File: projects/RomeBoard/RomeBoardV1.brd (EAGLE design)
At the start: 110 x 130 mm, 15 parts, among them J2 RASPBERRY-PI-HEADER

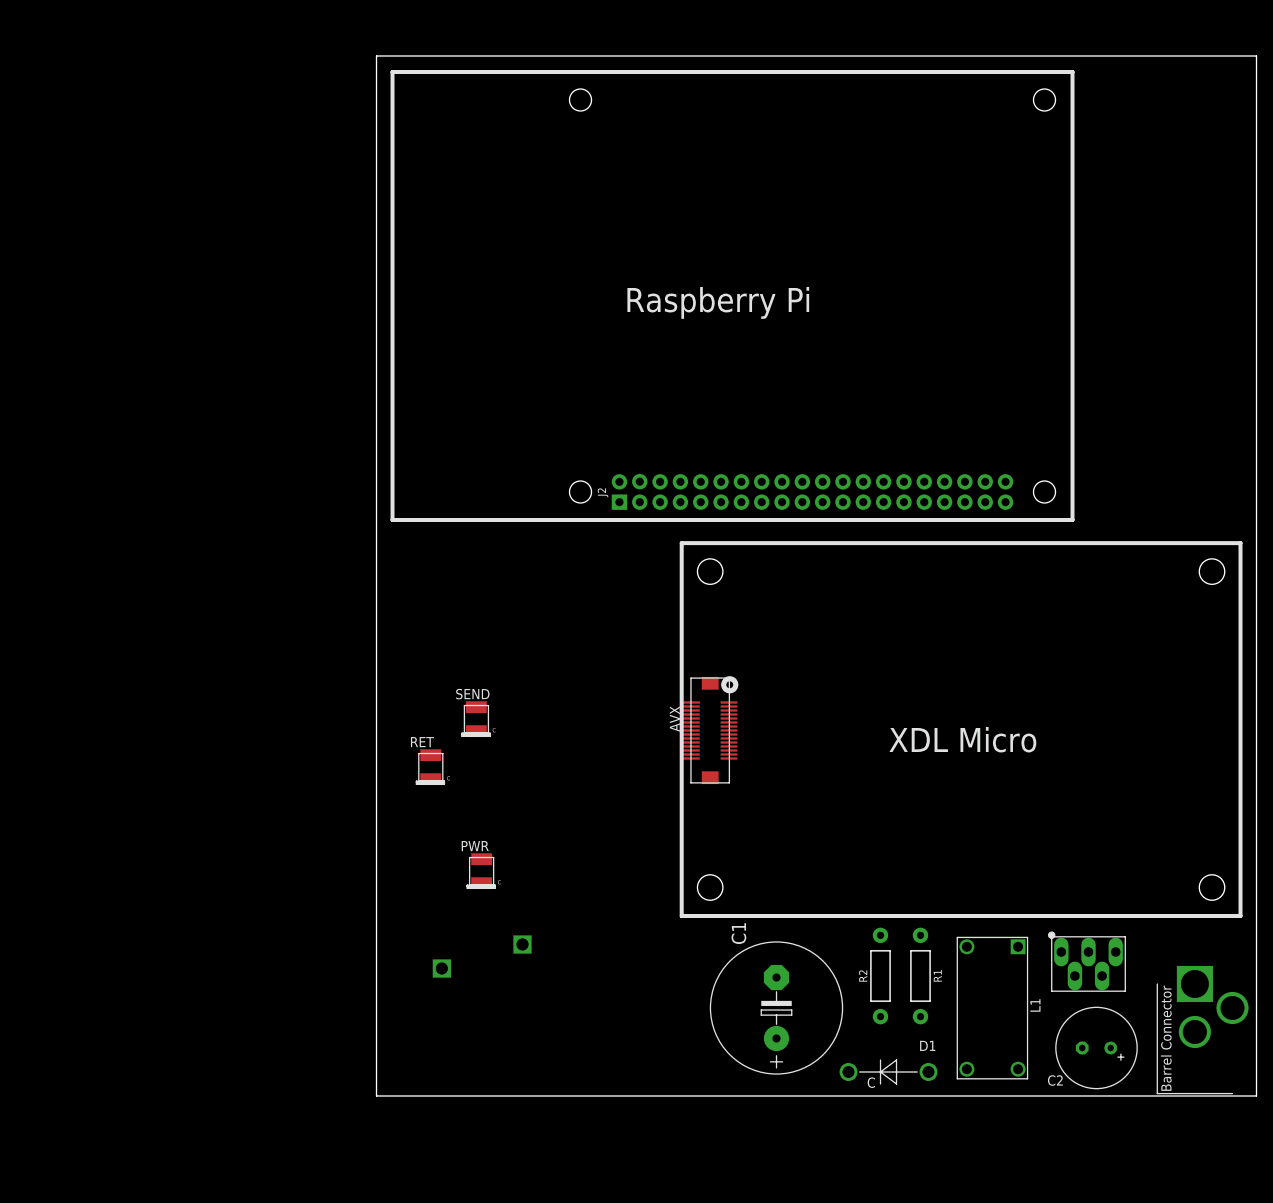
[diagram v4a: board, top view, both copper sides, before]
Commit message: Adding connectors + LED circuits
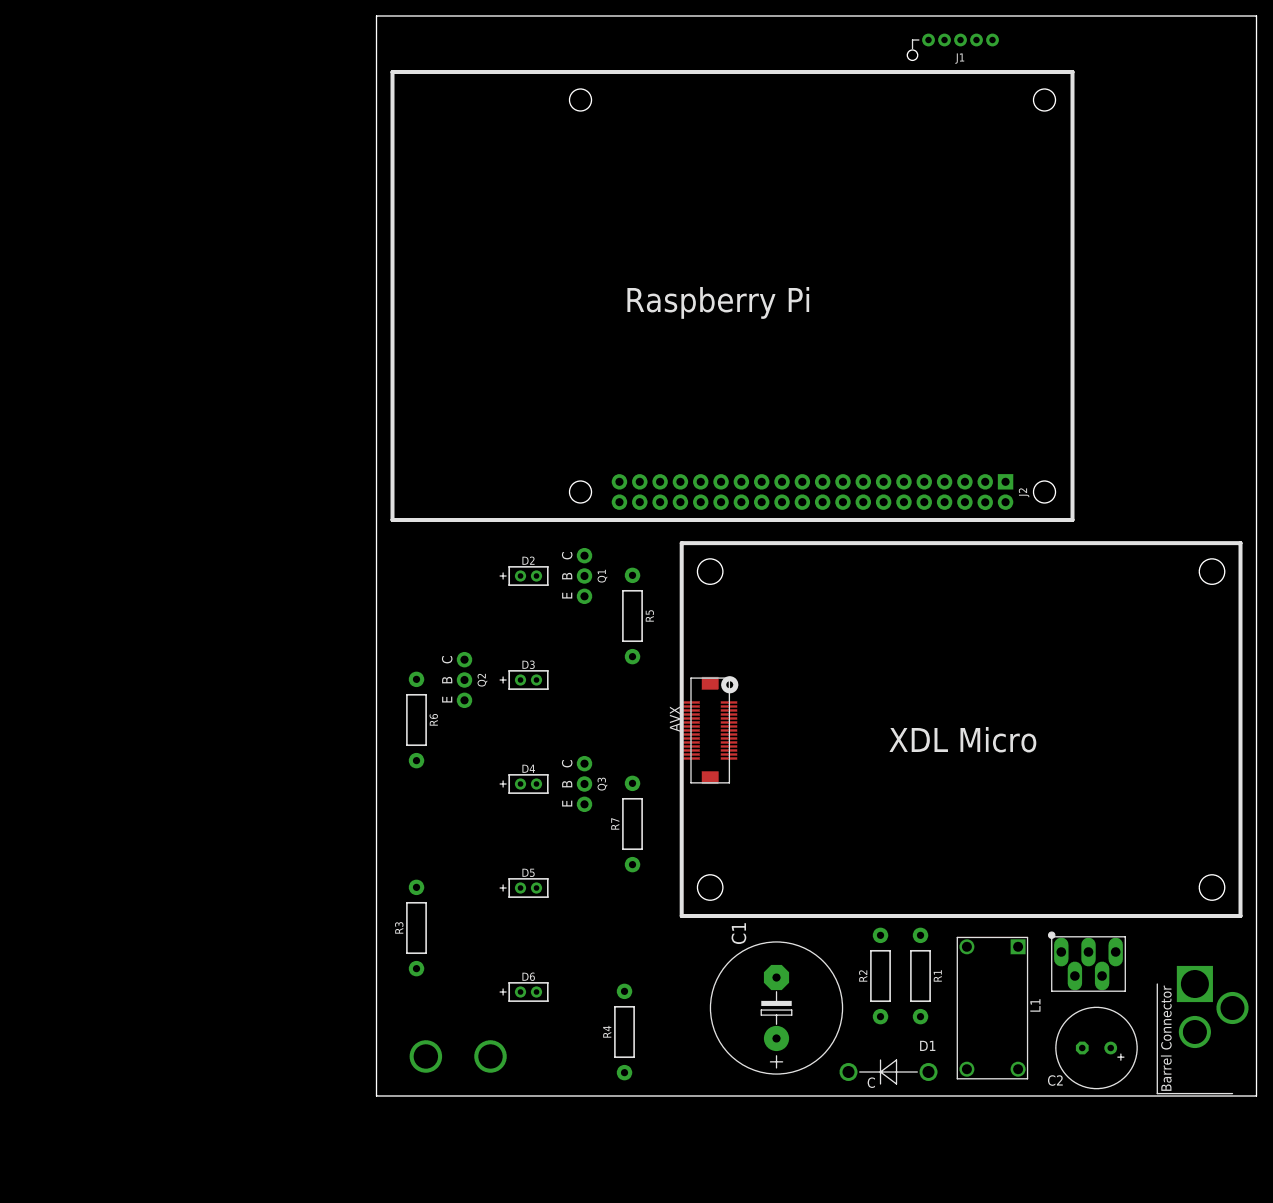
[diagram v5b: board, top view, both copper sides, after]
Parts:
- removed PWR, RET, SEND: LT-T673-Q1R2-25-Z, CNTRL_BOARD:PLCC-2
- added D2, D3, D4, D5, D6: LEDTHRU-HOLE-CONNECTOR, BrownSpaceEngineering:1X2-POL
- added J1: HEADER-5, BrownSpaceEngineering:HEADER-05
- added Q1, Q2, Q3: 2N4401, BrownSpaceEngineering:TO-923
- added R3: 100, passives:AXIAL-0.4
- added R4: 75, passives:AXIAL-0.4
- added R5, R6, R7: 89R, passives:AXIAL-0.4
- V4, V5: device BrownSpaceEngineering:VIA-60MIL-SQ -> BrownSpaceEngineering:VIA-120MIL
- moved V4 14.6 mm to (14.2, 4.94)
- moved V5 11.2 mm to (6.17, 4.94)
- turned J2 to 270 degrees
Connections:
- net P29 renamed !SHDN
- removed net P12: AVX.P12, PWR.A
- removed net P14: AVX.P14
- removed net P2: AVX.P2, SEND.A
- removed net P3: AVX.P3
- removed net P4: AVX.P4, RET.A
- new net N$10: D2.2, Q1.1
- new net N$2: D5.1, R3.2
- new net N$3: D6.1, R4.2
- new net N$4: D3.2, Q2.1
- new net N$5: Q1.3, R5.2
- new net N$6: Q2.3, R6.2
- new net N$7: Q3.3, R7.2
- new net N$9: D4.2, Q3.1
- new net PWR_L: AVX.P12, Q3.2
- new net RX_D: AVX.P14, J2.P10
- new net RX_L: AVX.P4, J2.P13, Q2.2
- new net TX_D: AVX.P3, J2.P8
- new net TX_L: AVX.P2, J2.P11, Q1.2
- net 3V6: now also R4.1
- net GND: now also D5.2, D6.2, J1.2, J1.3, J1.4, J1.5, J2.P14, J2.P20, J2.P25, J2.P30, J2.P34, J2.P39, J2.P6, J2.P9, R5.1, R6.1, R7.1; no longer PWR.C, RET.C, SEND.C
- net VIN: now also D2.1, D3.1, D4.1, J1.1, R3.1
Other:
- board size 110 x 130 mm -> 110 x 135 mm

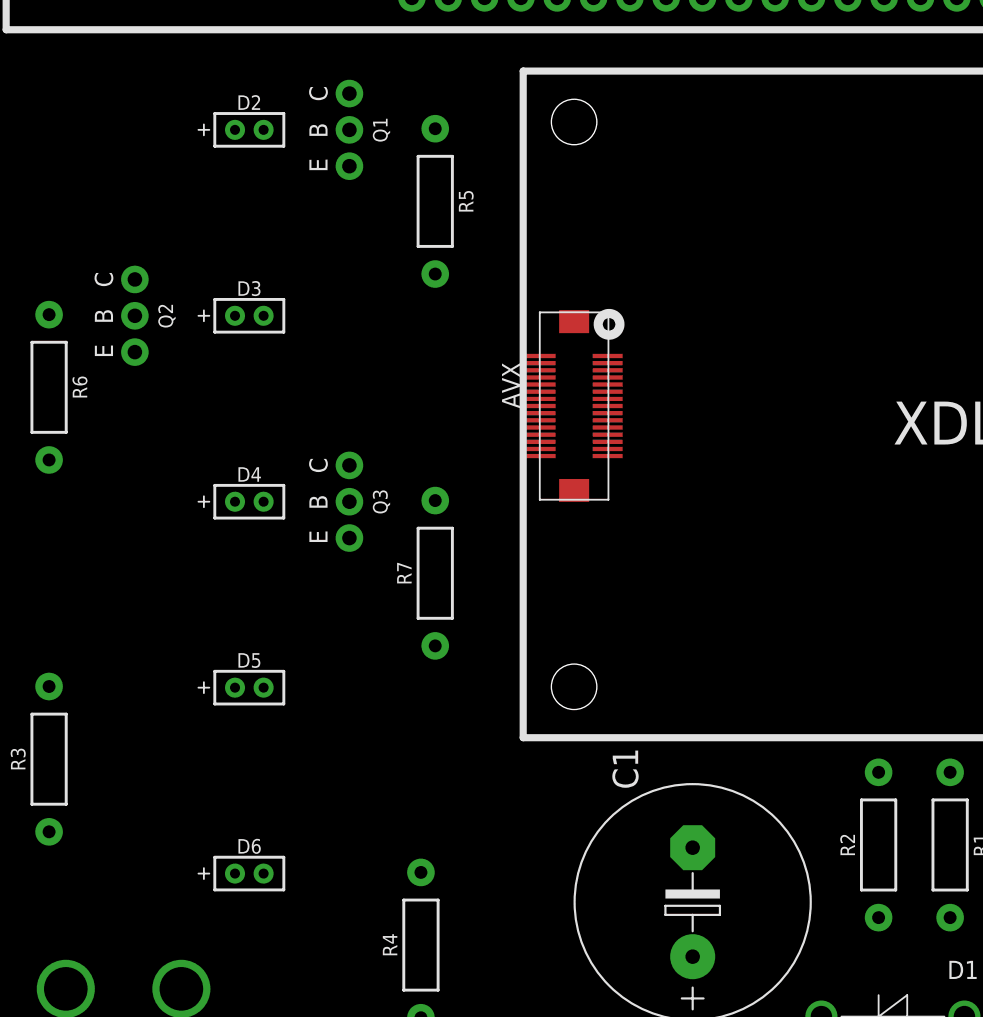
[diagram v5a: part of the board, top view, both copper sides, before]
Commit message: NPN -> NMOS
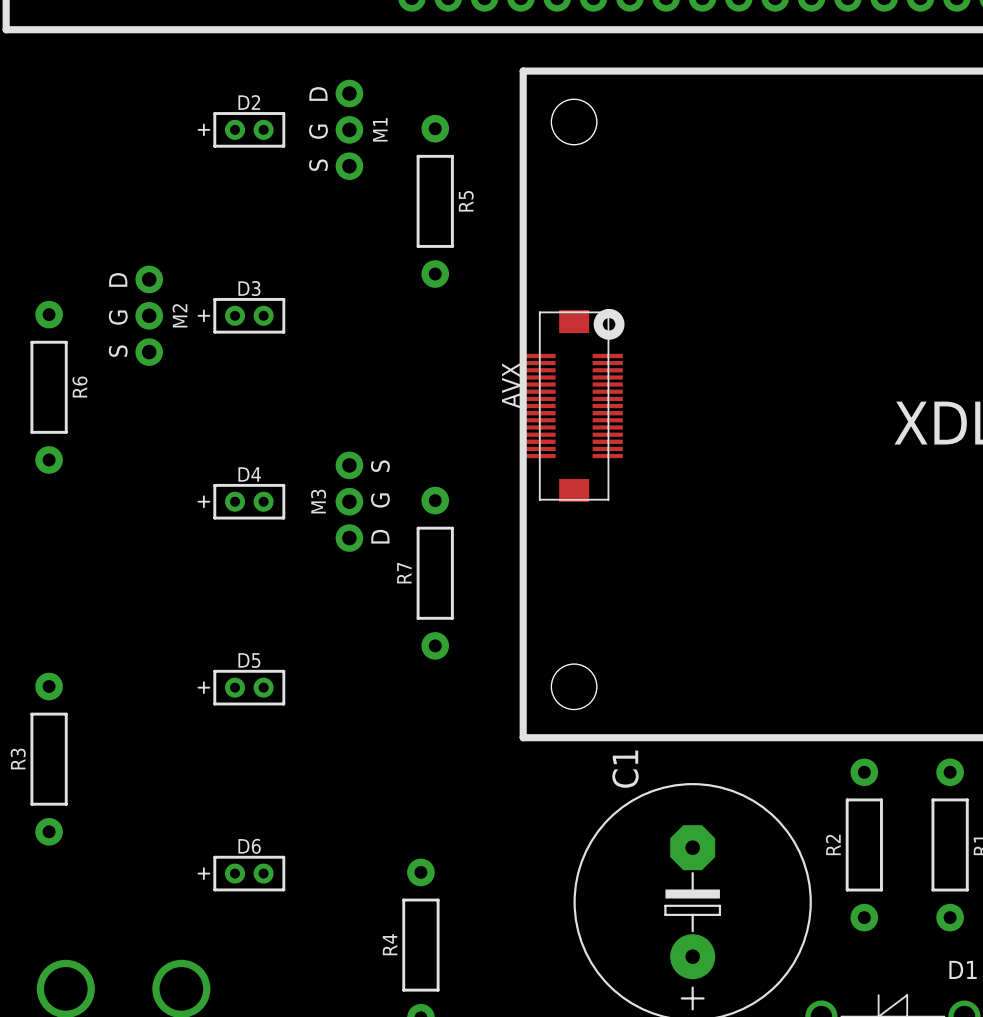
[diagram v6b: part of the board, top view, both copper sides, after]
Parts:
- removed Q1, Q2, Q3: 2N4401, BrownSpaceEngineering:TO-923
- added M1, M2, M3: 2N7000, BrownSpaceEngineering:TO-923-MOS
- R3: value 100 -> 100R
- R4: value 75 -> 75R
- R5, R6, R7: value 89R -> 147R
- moved R2 1.00 mm to (62.0, 15.0)
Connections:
- net GND: now also M1.3, M2.3, M3.3; no longer R5.1, R6.1, R7.1
- net N$10: now also R5.2; no longer Q1.1
- net N$4: now also R6.2; no longer Q2.1
- net N$5: now also M1.1, R5.1; no longer Q1.3, R5.2
- net N$6: now also M2.1, R6.1; no longer Q2.3, R6.2
- net N$7: now also M3.1, R7.1; no longer Q3.3, R7.2
- net N$9: now also R7.2; no longer Q3.1
- net PWR_L: now also M3.2; no longer Q3.2
- net RX_L: now also M2.2; no longer Q2.2
- net TX_L: now also M1.2; no longer Q1.2
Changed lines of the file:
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@@
 </element>
 <element name="R1" library="passives" package="AXIAL-0.4" value="5.76K" x="68" y="15" rot="R270"/>
-<element name="R2" library="passives" package="AXIAL-0.4" value="3K" x="63" y="15" rot="R90"/>
+<element name="R2" library="passives" package="AXIAL-0.4" value="3K" x="62" y="15" rot="R90"/>
 <element name="J2" library="BrownSpaceEngineering" package="HEADER-20X02" value="RASPBERRY-PI-HEADER" x="54.5" y="75.5" rot="R270"/>
 <element name="J1" library="BrownSpaceEngineering" package="HEADER-05" value="HEADER-5" x="73" y="132" rot="R180"/>
@@
 <attribute name="NAME" x="19" y="14.397" size="1.016" layer="25" font="vector" ratio="20" align="bottom-center"/>
 </element>
-<element name="R3" library="passives" package="AXIAL-0.4" value="100" x="5" y="21" rot="R90"/>
-<element name="R4" library="passives" package="AXIAL-0.4" value="75" x="31" y="8" rot="R90"/>
-<element name="Q1" library="BrownSpaceEngineering" package="TO-923" value="2N4401" x="26" y="65" rot="R270"/>
-<element name="Q2" library="BrownSpaceEngineering" package="TO-923" value="2N4401" x="11" y="52" rot="R270"/>
-<element name="Q3" library="BrownSpaceEngineering" package="TO-923" value="2N4401" x="26" y="39" rot="R270"/>
-<element name="R5" library="passives" package="AXIAL-0.4" value="89R" x="32" y="60" rot="R270"/>
-<element name="R6" library="passives" package="AXIAL-0.4" value="89R" x="5" y="47" rot="R270"/>
-<element name="R7" library="passives" package="AXIAL-0.4" value="89R" x="32" y="34" rot="R90"/>
+<element name="R3" library="passives" package="AXIAL-0.4" value="100R" x="5" y="21" rot="R90"/>
+<element name="R4" library="passives" package="AXIAL-0.4" value="75R" x="31" y="8" rot="R90"/>
+<element name="R5" library="passives" package="AXIAL-0.4" value="147R" x="32" y="60" rot="R270"/>
+<element name="R6" library="passives" package="AXIAL-0.4" value="147R" x="5" y="47" rot="R270"/>
+<element name="R7" library="passives" package="AXIAL-0.4" value="147R" x="32" y="34" rot="R90"/>
+<element name="M1" library="BrownSpaceEngineering" package="TO-923-MOS" value="2N7000" x="26" y="65" rot="R270"/>
+<element name="M2" library="BrownSpaceEngineering" package="TO-923-MOS" value="2N7000" x="12" y="52" rot="R270"/>
+<element name="M3" library="BrownSpaceEngineering" package="TO-923-MOS" value="2N7000" x="26" y="39" rot="R90"/>
 </elements>
 <signals>
@@
 <contactref element="D5" pad="2"/>
 <contactref element="D6" pad="2"/>
-<contactref element="R5" pad="1"/>
-<contactref element="R6" pad="1"/>
-<contactref element="R7" pad="1"/>
+<contactref element="M1" pad="3"/>
+<contactref element="M2" pad="3"/>
+<contactref element="M3" pad="3"/>
 <wire x1="73" y1="132" x2="75" y2="132" width="0" layer="19" extent="1-1"/>
 <wire x1="71" y1="132" x2="73" y2="132" width="0" layer="19" extent="1-1"/>
@@
 <wire x1="37.99" y1="74.23" x2="43.07" y2="74.23" width="0" layer="19" extent="1-1"/>
 <wire x1="30.37" y1="76.77" x2="37.99" y2="74.23" width="0" layer="19" extent="1-1"/>
-<wire x1="32" y1="65.08" x2="37.99" y2="74.23" width="0" layer="19" extent="1-1"/>
-<wire x1="44.06" y1="49.19" x2="32" y2="65.08" width="0" layer="19" extent="1-1"/>
+<wire x1="44.06" y1="49.19" x2="43.07" y2="74.23" width="0" layer="19" extent="1-1"/>
 <wire x1="44.06" y1="48.19" x2="44.06" y2="49.19" width="0" layer="19" extent="1-1"/>
 <wire x1="44.06" y1="47.69" x2="44.06" y2="48.19" width="0" layer="19" extent="1-1"/>
@@
 <wire x1="39.36" y1="44.69" x2="39.36" y2="44.19" width="0" layer="19" extent="1-1"/>
 <wire x1="39.36" y1="42.19" x2="39.36" y2="44.19" width="0" layer="19" extent="1-1"/>
-<wire x1="32" y1="28.92" x2="39.36" y2="42.19" width="0" layer="19" extent="1-1"/>
-<wire x1="20" y1="26" x2="32" y2="28.92" width="0" layer="19" extent="1-1"/>
+<wire x1="20" y1="26" x2="39.36" y2="42.19" width="0" layer="19" extent="1-1"/>
 <wire x1="20" y1="13" x2="20" y2="26" width="0" layer="19" extent="1-1"/>
 <wire x1="14.25" y1="4.94" x2="20" y2="13" width="0" layer="19" extent="1-1"/>
-<wire x1="50" y1="14.81" x2="32" y2="28.92" width="0" layer="19" extent="1-1"/>
-<wire x1="63" y1="9.92" x2="50" y2="14.81" width="0" layer="19" extent="1-1"/>
-<wire x1="69" y1="3" x2="63" y2="9.92" width="0" layer="19" extent="1-1"/>
+<wire x1="50" y1="14.81" x2="39.36" y2="42.19" width="0" layer="19" extent="1-1"/>
+<wire x1="62" y1="9.92" x2="50" y2="14.81" width="0" layer="19" extent="1-1"/>
+<wire x1="69" y1="3" x2="62" y2="9.92" width="0" layer="19" extent="1-1"/>
 <wire x1="88.222" y1="6" x2="69" y2="3" width="0" layer="19" extent="1-1"/>
 <wire x1="89" y1="18" x2="88.222" y2="6" width="0" layer="19" extent="1-1"/>
@@
 <wire x1="102.3" y1="8" x2="92.4" y2="18" width="0" layer="19" extent="1-1"/>
 <wire x1="107" y1="11" x2="102.3" y2="8" width="0" layer="19" extent="1-1"/>
-<wire x1="5" y1="52.08" x2="32" y2="65.08" width="0" layer="19" extent="1-1"/>
+<wire x1="26" y1="62.46" x2="14.25" y2="4.94" width="0" layer="19" extent="1-1"/>
+<wire x1="12" y1="49.46" x2="26" y2="62.46" width="0" layer="19" extent="1-1"/>
+<wire x1="26" y1="41.54" x2="12" y2="49.46" width="0" layer="19" extent="1-1"/>
 </signal>
 <signal name="3V6">
@@
 <contactref element="R2" pad="2"/>
 <wire x1="68" y1="20.08" x2="90.7" y2="15" width="0" layer="19" extent="1-1"/>
-<wire x1="63" y1="20.08" x2="68" y2="20.08" width="0" layer="19" extent="1-1"/>
+<wire x1="62" y1="20.08" x2="68" y2="20.08" width="0" layer="19" extent="1-1"/>
 </signal>
 <signal name="TX_L">
 <contactref element="AVX" pad="P2"/>
 <contactref element="J2" pad="P11"/>
-<contactref element="Q1" pad="2"/>
+<contactref element="M1" pad="2"/>
 <wire x1="39.36" y1="49.19" x2="65.93" y2="76.77" width="0" layer="19" extent="1-1"/>
 <wire x1="26" y1="65" x2="39.36" y2="49.19" width="0" layer="19" extent="1-1"/>
@@
 <contactref element="AVX" pad="P4"/>
 <contactref element="J2" pad="P13"/>
-<contactref element="Q2" pad="2"/>
+<contactref element="M2" pad="2"/>
 <wire x1="39.36" y1="48.69" x2="63.39" y2="76.77" width="0" layer="19" extent="1-1"/>
-<wire x1="11" y1="52" x2="39.36" y2="48.69" width="0" layer="19" extent="1-1"/>
+<wire x1="12" y1="52" x2="39.36" y2="48.69" width="0" layer="19" extent="1-1"/>
 </signal>
 <signal name="PWR_L">
 <contactref element="AVX" pad="P12"/>
-<contactref element="Q3" pad="2"/>
+<contactref element="M3" pad="2"/>
 <wire x1="26" y1="39" x2="39.36" y2="46.69" width="0" layer="19" extent="1-1"/>
 </signal>
@@
 <wire x1="18" y1="13" x2="31" y2="13.08" width="0" layer="19" extent="1-1"/>
 </signal>
-<signal name="N$5">
-<contactref element="R5" pad="2"/>
-<contactref element="Q1" pad="3"/>
-<wire x1="32" y1="54.92" x2="26" y2="62.46" width="0" layer="19" extent="1-1"/>
-</signal>
-<signal name="N$6">
-<contactref element="R6" pad="2"/>
-<contactref element="Q2" pad="3"/>
-<wire x1="5" y1="41.92" x2="11" y2="49.46" width="0" layer="19" extent="1-1"/>
-</signal>
-<signal name="N$7">
-<contactref element="R7" pad="2"/>
-<contactref element="Q3" pad="3"/>
-<wire x1="26" y1="36.46" x2="32" y2="39.08" width="0" layer="19" extent="1-1"/>
-</signal>
 <signal name="N$9">
 <contactref element="D4" pad="2"/>
-<contactref element="Q3" pad="1"/>
-<wire x1="20" y1="39" x2="26" y2="41.54" width="0" layer="19" extent="1-1"/>
+<contactref element="R7" pad="2"/>
+<wire x1="20" y1="39" x2="32" y2="39.08" width="0" layer="19" extent="1-1"/>
 </signal>
 <signal name="N$4">
 <contactref element="D3" pad="2"/>
-<contactref element="Q2" pad="1"/>
-<wire x1="11" y1="54.54" x2="20" y2="52" width="0" layer="19" extent="1-1"/>
+<contactref element="R6" pad="2"/>
+<wire x1="5" y1="41.92" x2="20" y2="52" width="0" layer="19" extent="1-1"/>
 </signal>
 <signal name="N$10">
 <contactref element="D2" pad="2"/>
-<contactref element="Q1" pad="1"/>
-<wire x1="20" y1="65" x2="26" y2="67.54" width="0" layer="19" extent="1-1"/>
+<contactref element="R5" pad="2"/>
+<wire x1="20" y1="65" x2="32" y2="54.92" width="0" layer="19" extent="1-1"/>
+</signal>
+<signal name="N$5">
+<contactref element="M1" pad="1"/>
+<contactref element="R5" pad="1"/>
+<wire x1="26" y1="67.54" x2="32" y2="65.08" width="0" layer="19" extent="1-1"/>
+</signal>
+<signal name="N$6">
+<contactref element="R6" pad="1"/>
+<contactref element="M2" pad="1"/>
+<wire x1="12" y1="54.54" x2="5" y2="52.08" width="0" layer="19" extent="1-1"/>
+</signal>
+<signal name="N$7">
+<contactref element="R7" pad="1"/>
+<contactref element="M3" pad="1"/>
+<wire x1="32" y1="28.92" x2="26" y2="36.46" width="0" layer="19" extent="1-1"/>
 </signal>
 </signals>
